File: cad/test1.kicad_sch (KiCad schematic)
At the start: 14 parts

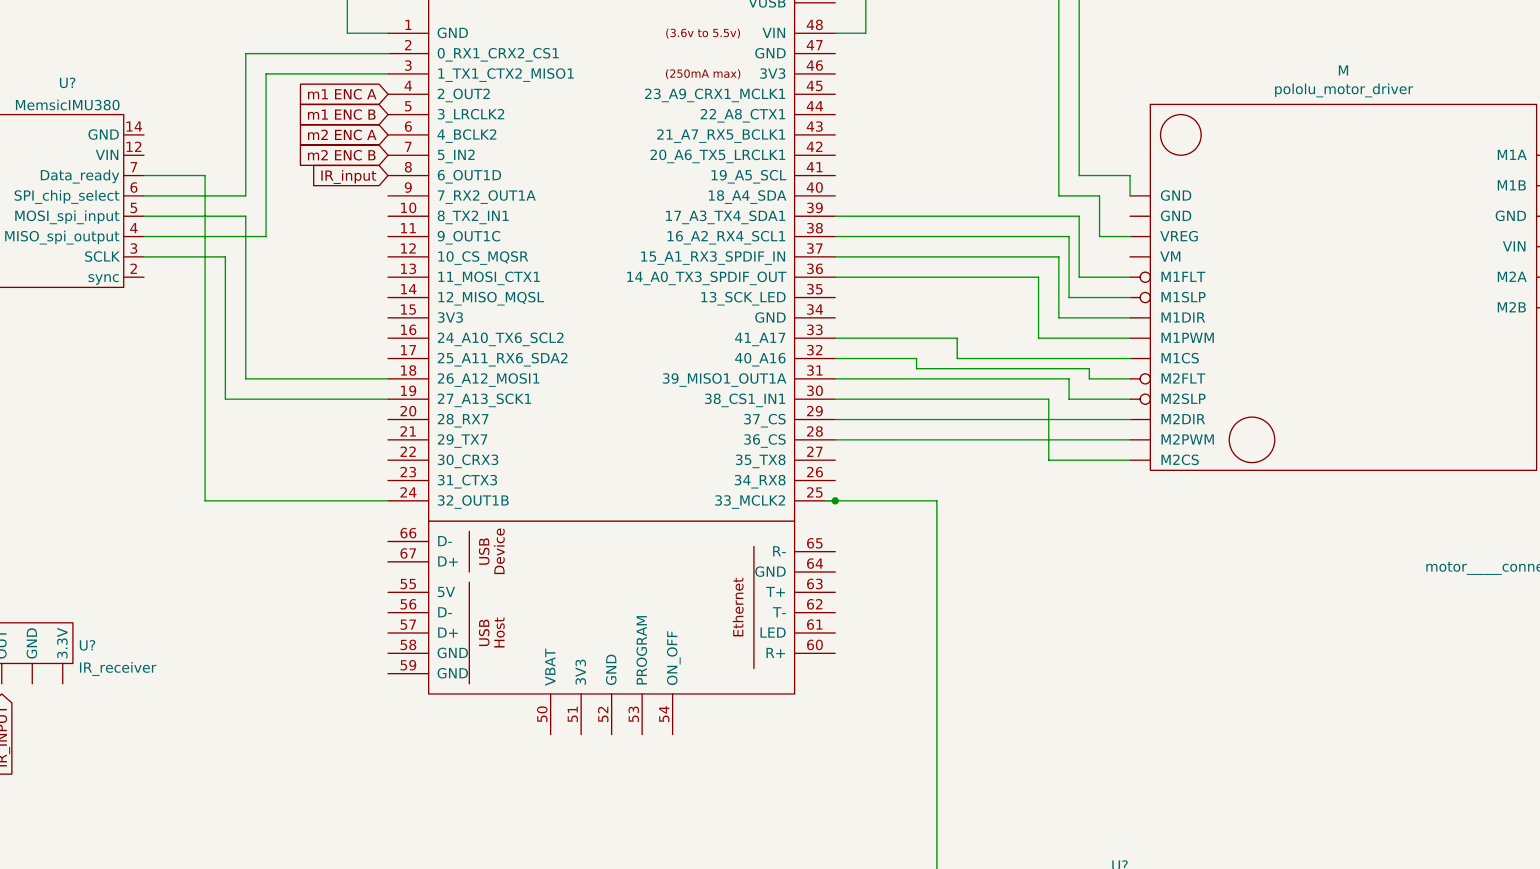
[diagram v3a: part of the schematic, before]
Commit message: memsic IMU working somehow
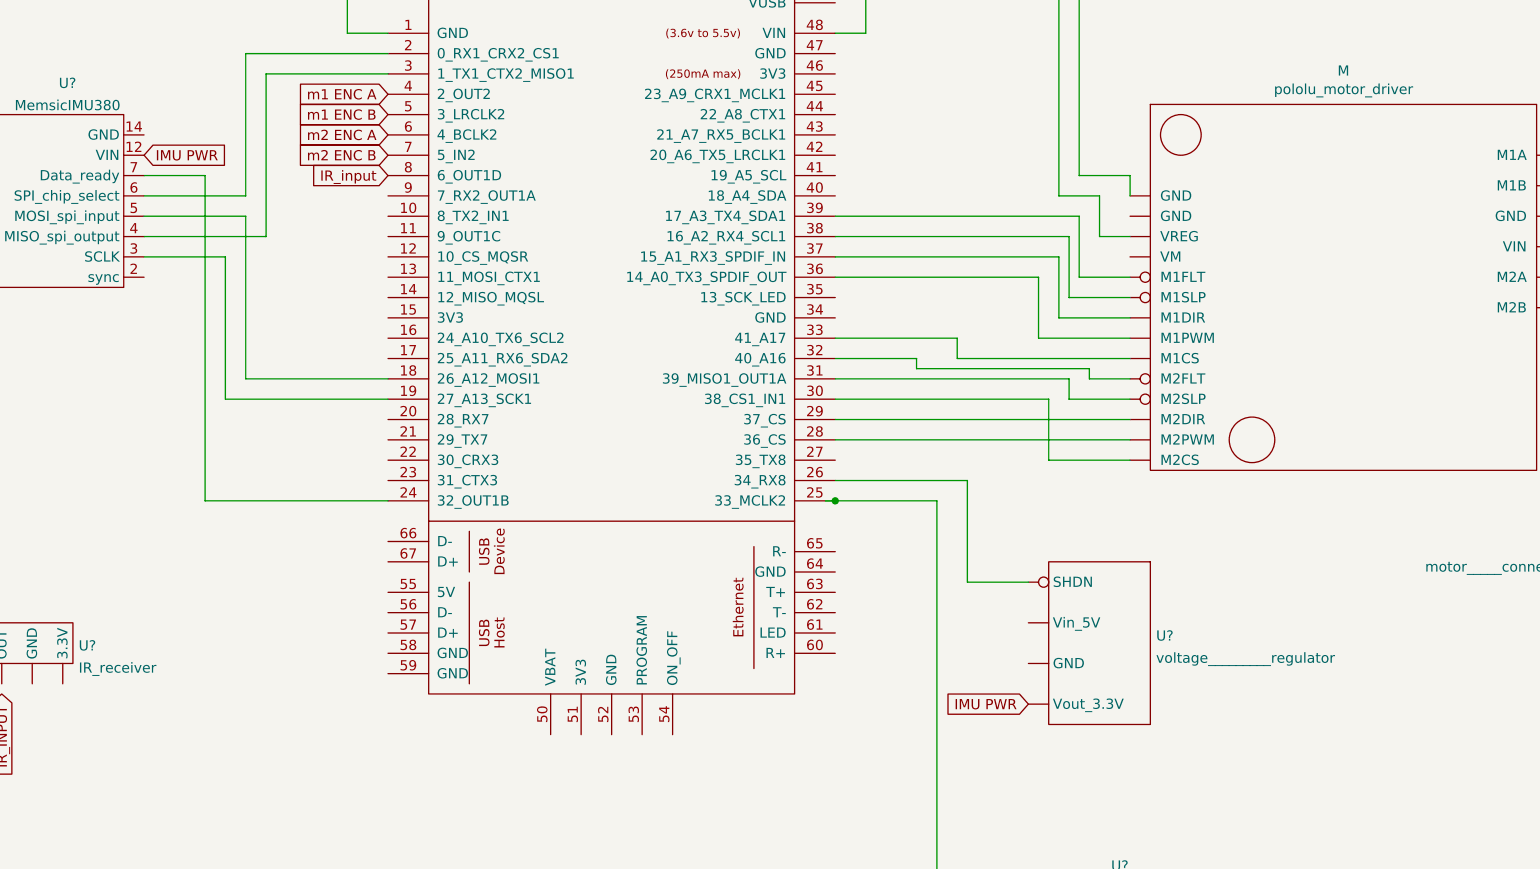
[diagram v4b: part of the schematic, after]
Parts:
- added U?: voltage_________regulator, symbol teetest:voltage_________regulator
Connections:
- net at U?.26 (34_RX8): now also U?. (Vout_3.3V)
- net at M.~ (VREG): now also BT?.2 (-)
- net at U?.-UB (Yellow_Enc_A): now also U?. (LV); no longer M.~ (VREG)
- net IMU PWR: now reaches U?.12 (VIN)
- net IMU PWR: now also U?. (Vout_3.3V)
- new net: M.~ (VREG), U?.-UB (Yellow_Enc_A)
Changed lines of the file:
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@@
+    (stroke (width 0) (type default) (color 0 0 0 0))
+  )
+  (wire (pts (xy 135.89 113.03) (xy 152.4 113.03))
     (stroke (width 0) (type default) (color 0 0 0 0))
   )
@@
   )
   (wire (pts (xy 151.13 97.79) (xy 151.13 95.25))
+    (stroke (width 0) (type default) (color 0 0 0 0))
+  )
+  (wire (pts (xy 152.4 113.03) (xy 152.4 125.73))
+    (stroke (width 0) (type default) (color 0 0 0 0))
+  )
+  (wire (pts (xy 152.4 125.73) (xy 160.02 125.73))
     (stroke (width 0) (type default) (color 0 0 0 0))
   )
@@
     )
   )
+  (global_label "IMU PWR" (shape input) (at 49.53 72.39 0) (fields_autoplaced)
+    (effects (font (size 1.27 1.27)) (justify left))
+    (property "Intersheet References" "${INTERSHEET_REFS}" (id 0) (at 60.2888 72.3106 0)
+      (effects (font (size 1.27 1.27)) (justify left) hide)
+    )
+  )
   (global_label "m1 ENC A" (shape input) (at 80.01 64.77 180) (fields_autoplaced)
     (effects (font (size 1.27 1.27)) (justify right))
@@
     (effects (font (size 1.27 1.27)) (justify right))
     (property "Intersheet References" "${INTERSHEET_REFS}" (id 0) (at 152.2245 167.5606 0)
+      (effects (font (size 1.27 1.27)) (justify right) hide)
+    )
+  )
+  (global_label "IMU PWR" (shape input) (at 160.02 140.97 180) (fields_autoplaced)
+    (effects (font (size 1.27 1.27)) (justify right))
+    (property "Intersheet References" "${INTERSHEET_REFS}" (id 0) (at 149.2612 140.8906 0)
       (effects (font (size 1.27 1.27)) (justify right) hide)
     )
@@
     (pin "1")
     (pin "2")
+  )
+  (symbol (lib_id "teetest:voltage_________regulator") (at 177.8 133.35 270) (unit 1)
+    (in_bom yes) (on_board yes) (fields_autoplaced)
+    (property "Reference" "U?" (id 0) (at 175.9713 132.4415 90)
+      (effects (font (size 1.27 1.27)) (justify left))
+    )
+    (property "Value" "voltage_________regulator" (id 1) (at 175.9713 135.2166 90)
+      (effects (font (size 1.27 1.27)) (justify left))
+    )
+    (property "Footprint" "" (id 2) (at 177.8 133.35 0)
+      (effects (font (size 1.27 1.27)) hide)
+    )
+    (property "Datasheet" "" (id 3) (at 177.8 133.35 0)
+      (effects (font (size 1.27 1.27)) hide)
+    )
+    (pin "")
+    (pin "")
+    (pin "")
+    (pin "")
   )
   (symbol (lib_id "teetest:logic_level_shifter") (at 284.48 76.2 0) (mirror y) (unit 1)
@@
       (reference "U?") (unit 1) (value "IR_receiver") (footprint "")
     )
+    (path "/1e333771-6350-4211-907d-e3023442de88"
+      (reference "U?") (unit 1) (value "voltage_________regulator") (footprint "")
+    )
     (path "/4e500e13-ea9a-40b7-b159-45969c12dcd2"

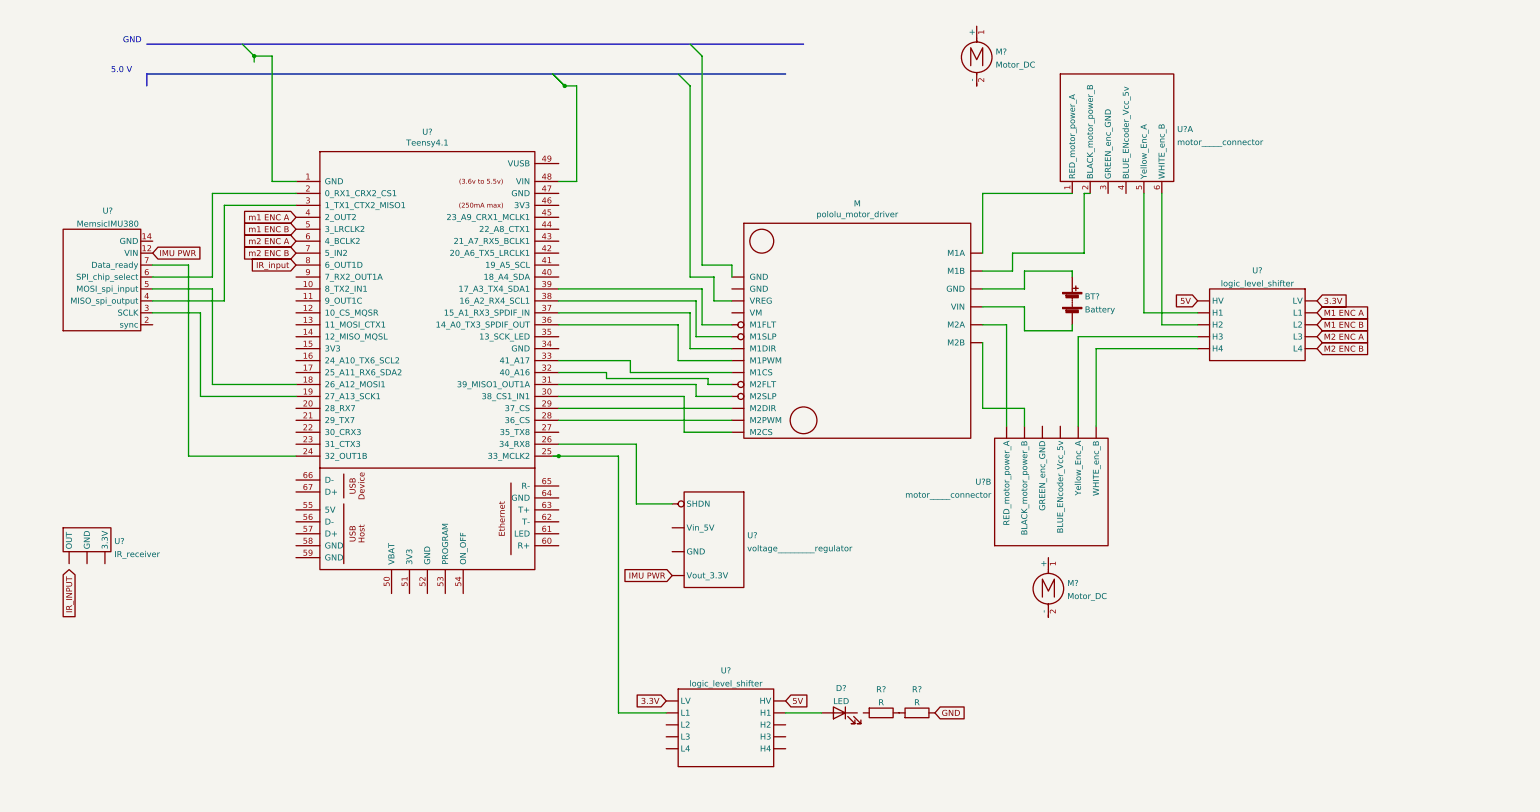
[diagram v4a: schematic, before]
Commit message: + main batt power check
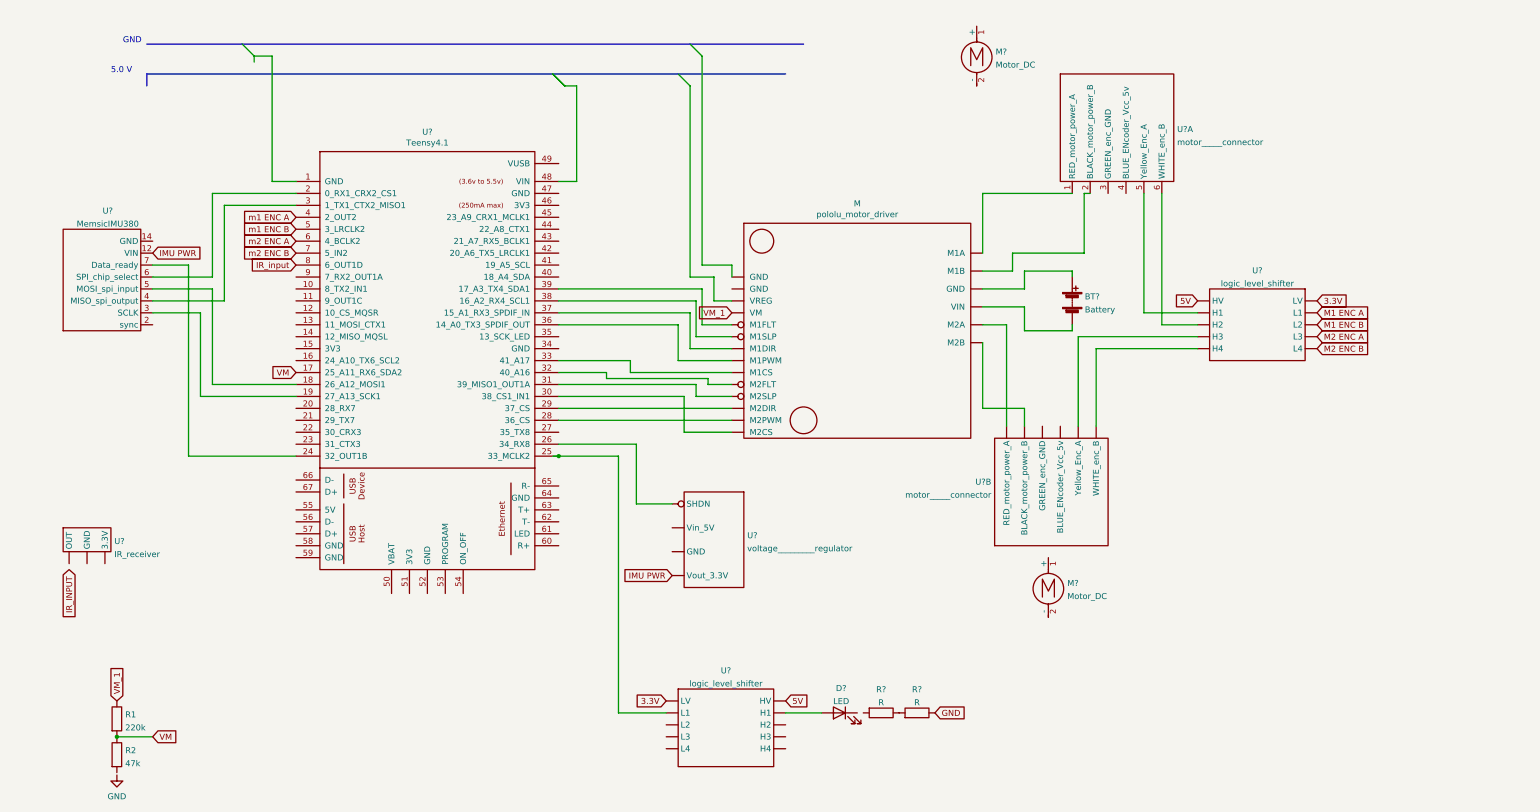
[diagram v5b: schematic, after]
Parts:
- added R1: 220k, symbol Device:R
- added R2: 47k, symbol Device:R
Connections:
- net VM: now reaches U?.17 (25_A11_RX6_SDA2)
- net VM: now also R1.2, R2.1
- net VM_1: now reaches M.~ (VREG)
- net VM_1: now also R1.1
- net at U?.-UB (Yellow_Enc_A): now also U?. (LV); no longer M.~ (VREG)
- new net: M.~ (VREG), U?.-UB (Yellow_Enc_A)
